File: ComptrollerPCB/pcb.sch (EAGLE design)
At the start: 35 parts, among them J1 FEMALE_HEADER_5X2, U1 ATMEGA32U4, X1 16MHz

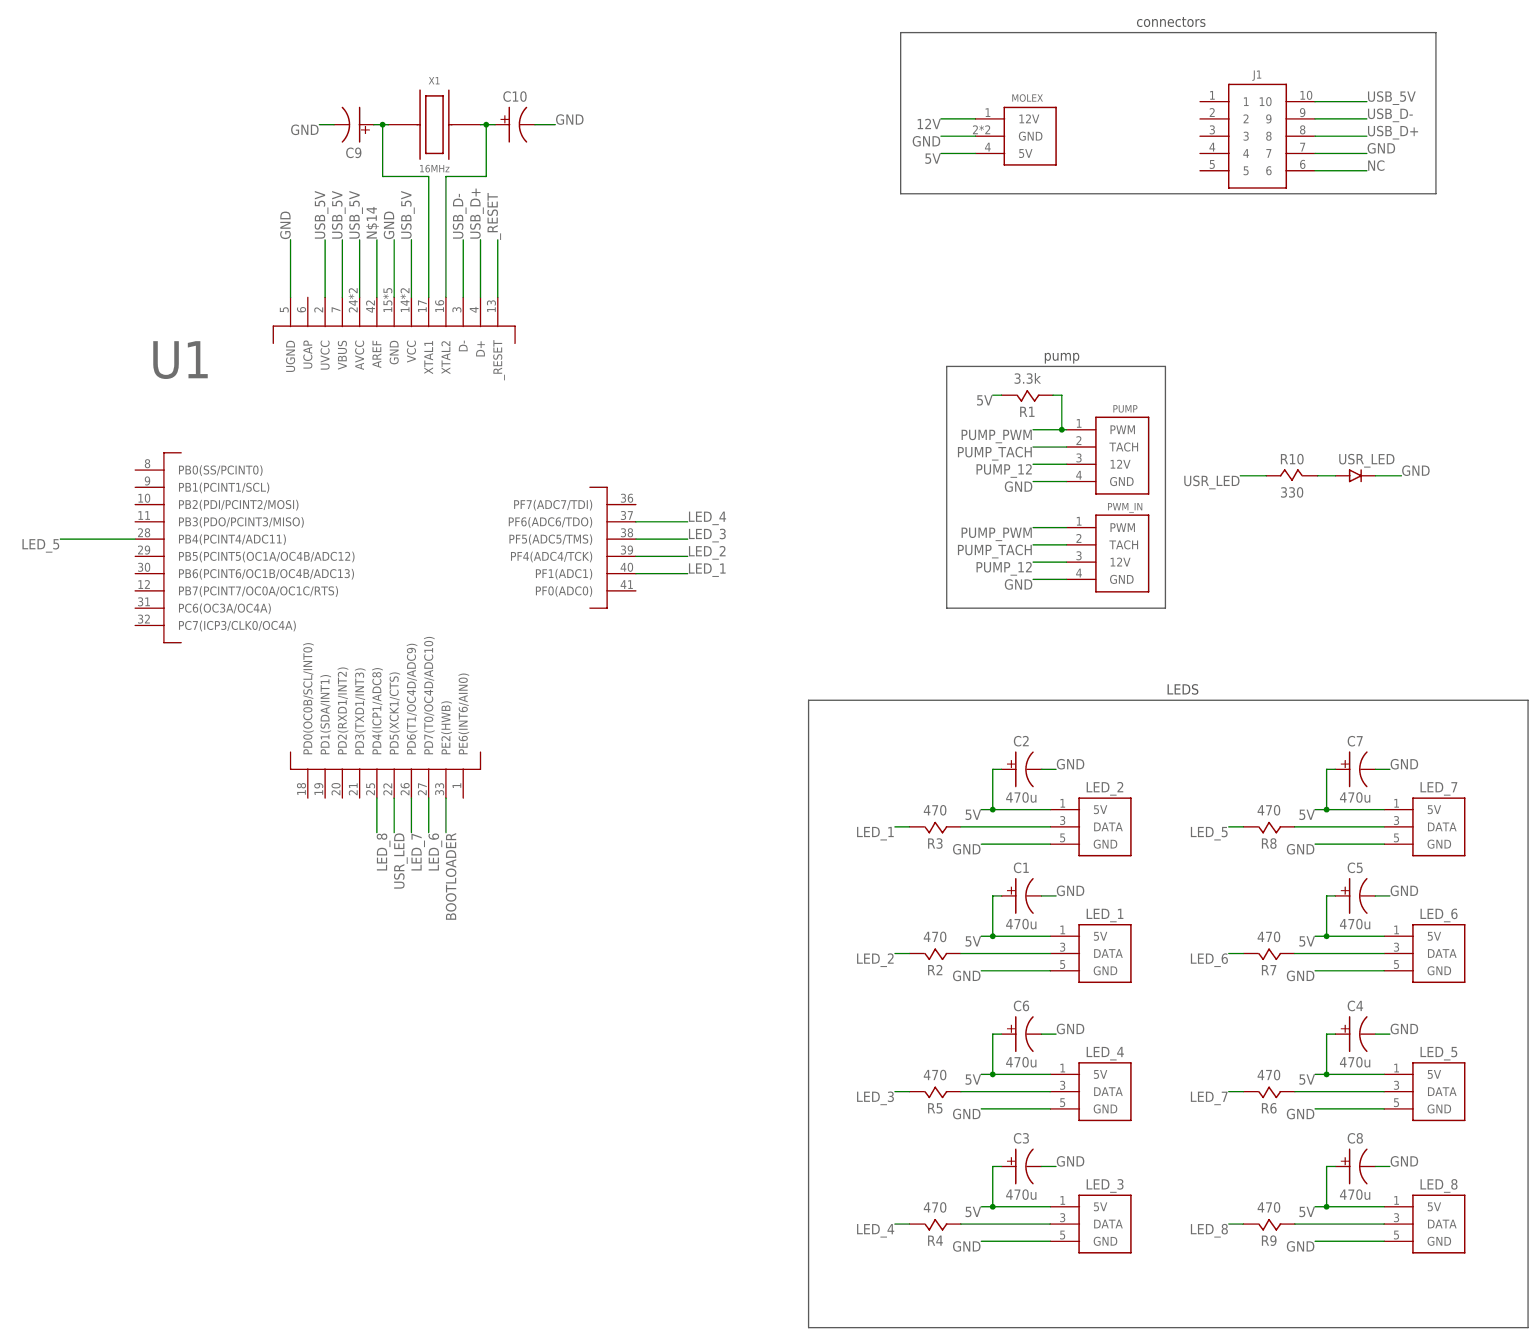
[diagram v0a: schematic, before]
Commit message: analog additions to read temperatures
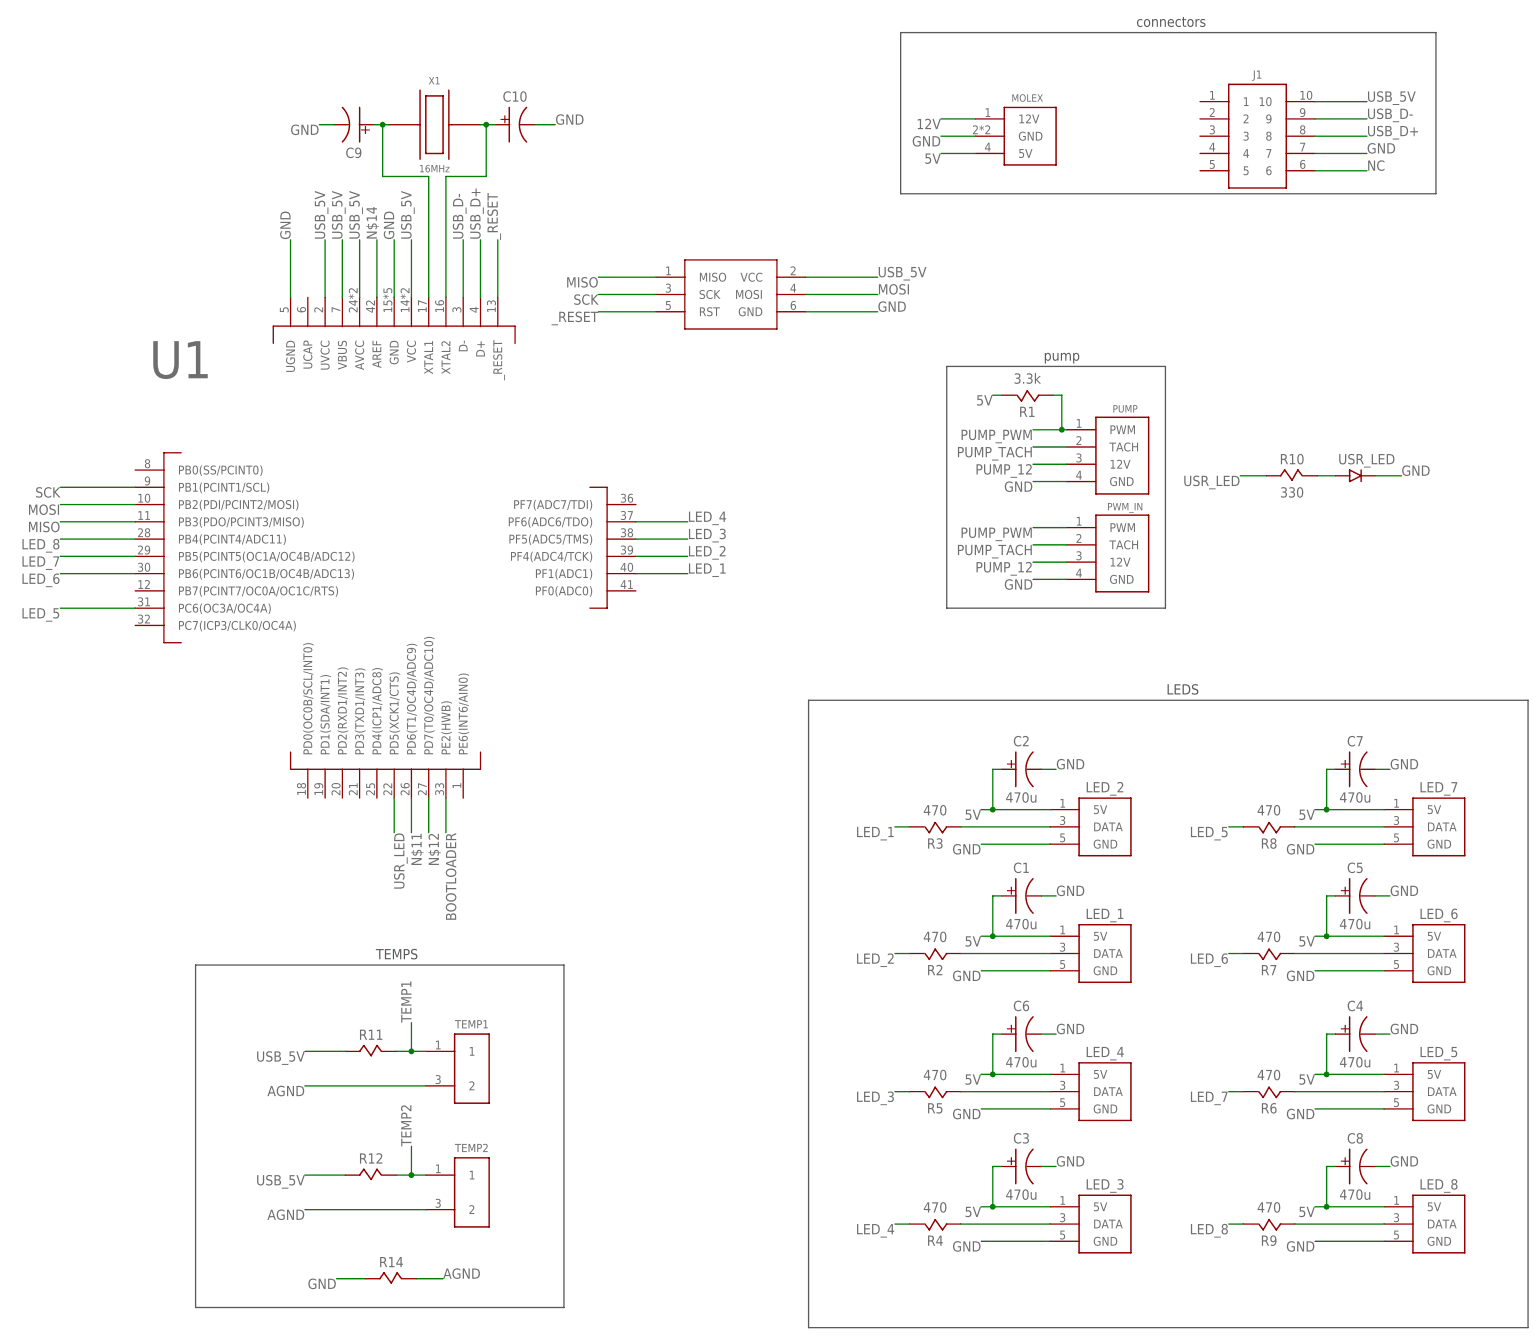
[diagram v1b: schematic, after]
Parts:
- added J2: ISP_CONN_6PIN, connectors:ISP_CONN_6PIN
- added R11, R12, R14: (no value), passive:RESISTOR
- added TEMP1, TEMP2: FEMALE_HEADER_2X1, connectors:FEMALE_HEADER_2X1
- J1: value FEMALE_HEADER_5X2 -> FEMALE_HEADER_5X2SMT; device connectors:FEMALE_HEADER_5X2 -> connectors:FEMALE_HEADER_5X2SMT
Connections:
- new net AGND: R14.2, TEMP1.2, TEMP2.2
- new net MISO: J2.MISO, U1.PB3(PDO/PCINT3/MISO)
- new net MOSI: J2.MOSI, U1.PB2(PDI/PCINT2/MOSI)
- new net N$11: U1.PD6(T1/OC4D/ADC9)
- new net N$12: U1.PD7(T0/OC4D/ADC10)
- new net SCK: J2.SCK, U1.PB1(PCINT1/SCL)
- new net TEMP1: R11.2, TEMP1.1
- new net TEMP2: R12.2, TEMP2.1
- net GND: now also J2.GND, R14.1
- net LED_5: now also U1.PC6(OC3A/OC4A); no longer U1.PB4(PCINT4/ADC11)
- net LED_6: now also U1.PB6(PCINT6/OC1B/OC4B/ADC13); no longer U1.PD7(T0/OC4D/ADC10)
- net LED_7: now also U1.PB5(PCINT5(OC1A/OC4B/ADC12); no longer U1.PD6(T1/OC4D/ADC9)
- net LED_8: now also U1.PB4(PCINT4/ADC11); no longer U1.PD4(ICP1/ADC8)
- net USB_5V: now also J2.VCC, R11.1, R12.1
- net _RESET: now also J2.RST
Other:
- note added: "TEMPS"
